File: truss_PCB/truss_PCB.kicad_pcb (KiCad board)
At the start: 2 copper layers, 114.3 x 102.9 mm, 195 parts, among them IC1 BAJ0BC0FP-E2, J1 XT60_60A_male, J10 IN_B, J11 IN_B, J12 Serial IO, J13 IO Header, J14 LV IO, J15 HV IO, J2 LimitSwitch, J3 Servo, J4 Truss Connection, J5 IN_B, J6 IN_B, J7 IN_B, J8 IN_B, J9 IN_B, Q1 BC807, Q2 BC807, Q3 BC807, Q4 BC807, Q5 BC807, Q6 BC807, Q7 BC807, Q8 IRF5305_PBF, U1 HX711, U11 LM2596S-ADJ, U12 AMS1117-5.0, U13 AMS1117-3.3, U2 HX711, U3 HX711, U4 HX711, U5 HX711, U6 HX711, U7 HX711, U8 TXS0108EPW, U9 TXS0108EPW

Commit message: updating truss PCB
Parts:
- removed C28: 680u, Capacitor_SMD:CP_Elec_10x10
- added EC28: 680u, Capacitor_SMD:CP_Elec_10x10, F.Cu at (134.6, 60.8)
- added J16: GND, Connector_PinHeader_2.54mm:PinHeader_1x03_P2.54mm_Vertical, F.Cu at (127.6, 99.7)
- added J17: GND, Connector_PinHeader_2.54mm:PinHeader_1x03_P2.54mm_Vertical, F.Cu at (132.7, 95.9)
- added J18: 12V, Connector_PinHeader_2.54mm:PinHeader_1x01_P2.54mm_Vertical, F.Cu at (141.0, 70.5)
- added J19: 6V, Connector_PinHeader_2.54mm:PinHeader_1x01_P2.54mm_Vertical, F.Cu at (141.0, 81.9)
- added J20: 5V_MCU, Connector_PinHeader_2.54mm:PinHeader_1x01_P2.54mm_Vertical, F.Cu at (141.0, 78.1)
- added J21: 3V3, Connector_PinHeader_2.54mm:PinHeader_1x01_P2.54mm_Vertical, F.Cu at (141.0, 85.7)
- added J22: 10V, Connector_PinHeader_2.54mm:PinHeader_1x01_P2.54mm_Vertical, F.Cu at (141.0, 74.3)
- added R47: 10k, Resistor_SMD:R_0805_2012Metric_Pad1.20x1.40mm_HandSolder, F.Cu at (149.9, 123.8)
- added R48: 10k, Resistor_SMD:R_0805_2012Metric_Pad1.20x1.40mm_HandSolder, F.Cu at (149.9, 126.4)
- added R49: 10k, Resistor_SMD:R_0805_2012Metric_Pad1.20x1.40mm_HandSolder, F.Cu at (149.9, 128.9)
- added R50: 10k, Resistor_SMD:R_0805_2012Metric_Pad1.20x1.40mm_HandSolder, F.Cu at (149.9, 131.4)
- added R51: 10k, Resistor_SMD:R_0805_2012Metric_Pad1.20x1.40mm_HandSolder, F.Cu at (149.9, 134.0)
- J3: footprint Connector_PinHeader_2.54mm:PinHeader_1x03_P2.54mm_Vertical -> Connector_PinHeader_2.54mm:PinHeader_1x01_P2.54mm_Vertical
- N2: moved to B.Cu
- moved D5 7.58 mm to (151.1, 81.9)
- moved D8 7.48 mm to (151.1, 85.7)
- moved D7 7.40 mm to (151.1, 78.1)
- moved D3 7.23 mm to (151.1, 70.5)
- moved D6 7.23 mm to (151.1, 74.3)
- moved JP39 4.44 mm to (151.1, 118.7)
- moved JP38 4.43 mm to (156.2, 118.7)
- moved R43 2.86 mm to (147.1, 85.7)
- moved R40 2.84 mm to (147.0, 81.9)
- moved R42 2.53 mm to (147.1, 78.1)
- moved R41 2.44 mm to (147.1, 74.3)
- moved R39 2.35 mm to (147.1, 70.5)
- moved JP29 0.62 mm to (161.9, 122.6)
- moved G*** 0.51 mm to (144.3, 92.7)
- moved N2 0.43 mm to (156.7, 65.4)
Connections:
- net Net-(A1-Pad1) renamed /MCU/TX
- net Net-(A1-Pad2) renamed /MCU/RX
- A1 pad 24: Net-(A1-Pad24) -> /MCU/LED_2
- A1 pad 25: Net-(A1-Pad25) -> /MCU/LED_3
- A1 pad 26: Net-(A1-Pad26) -> /MCU/LED_4
- D10 pad 2: Net-(A1-Pad25) -> /MCU/LED_3
- D11 pad 2: Net-(A1-Pad26) -> /MCU/LED_4
- D3 pad 1: Net-(D3-Pad1) -> GNDPWR
- D3 pad 2: /Power Distribution/12V_BUS -> Net-(D3-Pad2)
- D5 pad 1: Net-(D5-Pad1) -> GNDPWR
- D5 pad 2: /SERVO_POWER -> Net-(D5-Pad2)
- D6 pad 1: Net-(D6-Pad1) -> GNDPWR
- D6 pad 2: /10V_DC -> Net-(D6-Pad2)
- D7 pad 1: Net-(D7-Pad1) -> GNDPWR
- D7 pad 2: 5VDC -> Net-(D7-Pad2)
- D8 pad 1: Net-(D8-Pad1) -> GNDPWR
- D8 pad 2: 3V3DC -> Net-(D8-Pad2)
- D9 pad 2: Net-(A1-Pad24) -> /MCU/LED_2
- J13 pad 5: Net-(A1-Pad24) -> /MCU/LED_2
- J13 pad 6: Net-(A1-Pad25) -> /MCU/LED_3
- J13 pad 7: Net-(A1-Pad26) -> /MCU/LED_4
- J3 pad 1: /SERVO_PWM -> /SERVO_POWER
- J4 pad 15: unconnected-(J4-Pad15) -> /MCU/SPARE_0
- J4 pad 16: unconnected-(J4-Pad16) -> /MCU/LED_3
- J4 pad 34: unconnected-(J4-Pad34) -> /MCU/LED_2
- J4 pad 35: unconnected-(J4-Pad35) -> /MCU/LED_4
- R39 pad 1: GNDPWR -> Net-(D3-Pad2)
- R39 pad 2: Net-(D3-Pad1) -> /Power Distribution/12V_BUS
- R40 pad 1: GNDPWR -> Net-(D5-Pad2)
- R40 pad 2: Net-(D5-Pad1) -> /SERVO_POWER
- R41 pad 1: GNDPWR -> Net-(D6-Pad2)
- R41 pad 2: Net-(D6-Pad1) -> /10V_DC
- R42 pad 1: GNDPWR -> Net-(D7-Pad2)
- R42 pad 2: Net-(D7-Pad1) -> 5VDC
- R43 pad 1: GNDPWR -> Net-(D8-Pad2)
- R43 pad 2: Net-(D8-Pad1) -> 3V3DC
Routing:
- net GNDPWR: track 162.2 -> 316.5 mm, vias 41 -> 39
- net /SERVO_GND: track 175.9 -> 24.1 mm
- net Net-(A1-Pad24): track 14.7 -> 0.00 mm
- net /MCU/LED_2: track 0.00 -> 14.7 mm
- net Net-(A1-Pad25): track 14.4 -> 0.00 mm
- net /MCU/LED_3: track 0.00 -> 14.4 mm
- net Net-(A1-Pad26): track 14.1 -> 0.00 mm
- net /MCU/LED_4: track 0.00 -> 14.1 mm
- net Net-(J14-Pad1): track 9.14 -> 15.0 mm
- net Net-(J14-Pad5): track 3.60 -> 9.47 mm
- net Net-(J14-Pad4): track 4.16 -> 10.0 mm
- net Net-(J14-Pad3): track 5.36 -> 11.2 mm
- net Net-(J14-Pad2): track 7.25 -> 13.1 mm
- net 5VDC: track 470.6 -> 475.9 mm
- net /10V_DC: track 205.5 -> 210.8 mm
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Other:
- board text added: "LABEL THESE"
- board text added: "RST"
- board text added: "Rx"
- board text added: "Tx"
- board text added: "Vusb"

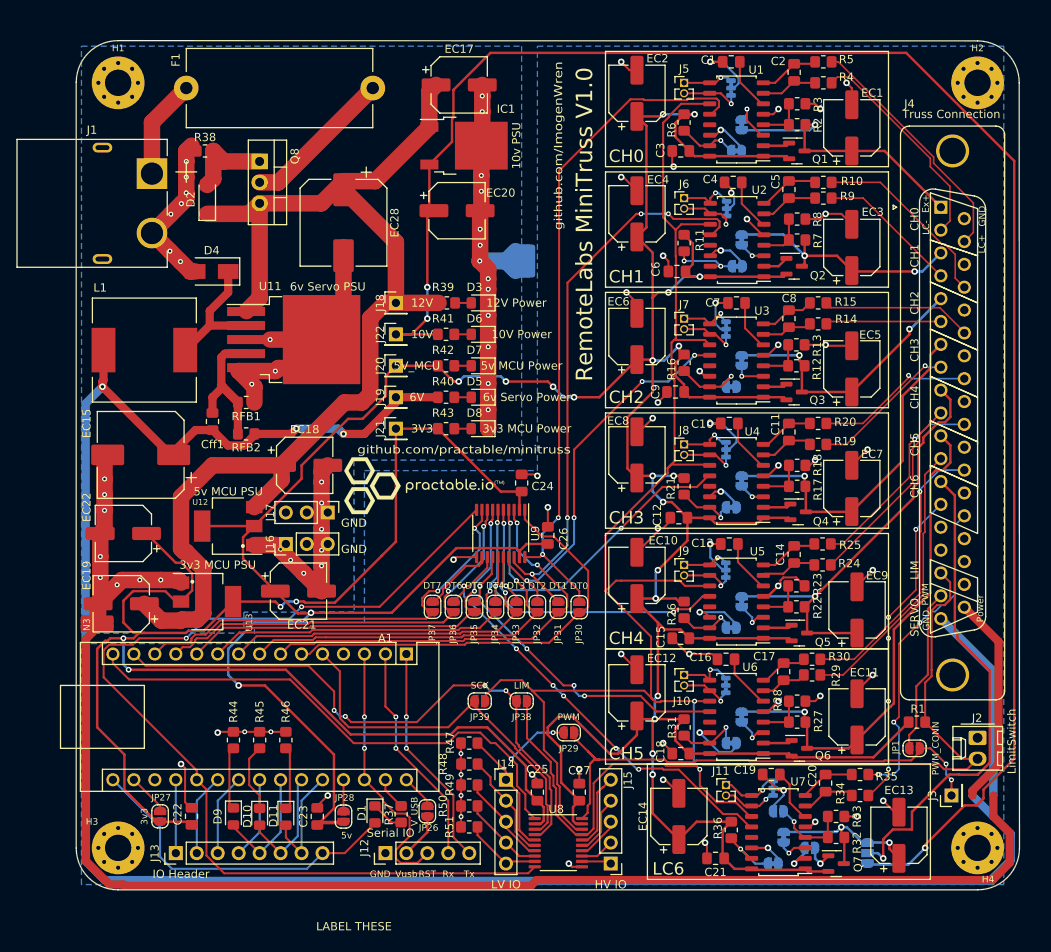
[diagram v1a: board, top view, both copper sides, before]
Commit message: Board V2 Almost Finished TODO# RUN DRC
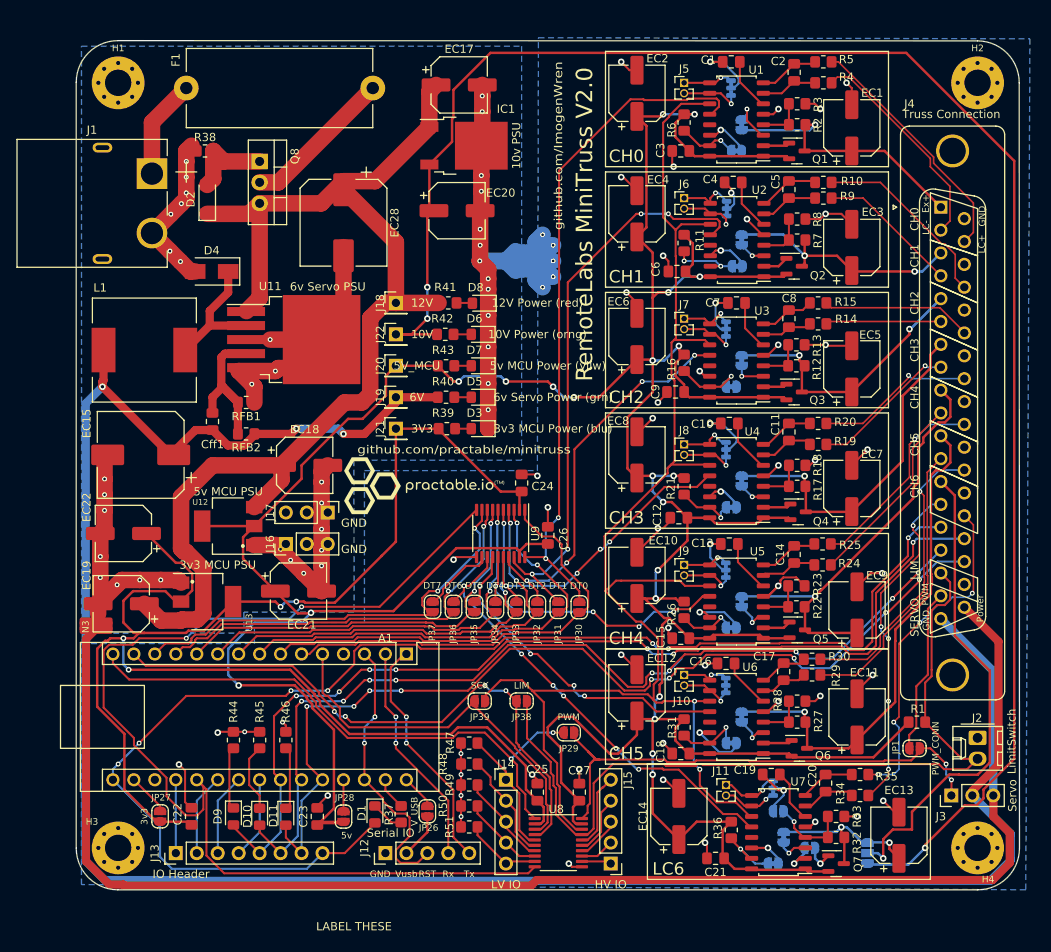
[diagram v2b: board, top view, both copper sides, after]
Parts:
- D3: value 12V Power -> 3v3 MCU Power (blu)
- D5: value 6v Servo Power -> 6v Servo Power (grn)
- D6: value 10V Power -> 10V Power (orng)
- D7: value 5v MCU Power -> 5v MCU Power (yllw)
- D8: value 3v3 MCU Power -> 12V Power (red)
- J3: footprint Connector_PinHeader_2.54mm:PinHeader_1x01_P2.54mm_Vertical -> Connector_PinHeader_2.54mm:PinHeader_1x03_P2.54mm_Vertical
- R39: value 10k -> 330r
- R40: value 1k -> 10k
- R42: value 1k -> 8k2
- R43: value 330r -> 1k
- moved D3 15.2 mm to (151.1, 85.7)
- moved R39 15.2 mm to (147.1, 85.7)
- moved D8 15.2 mm to (151.3, 70.5)
- moved R43 7.62 mm to (147.1, 78.1)
- moved R41 3.82 mm to (147.3, 70.5)
- moved R42 3.81 mm to (147.0, 74.3)
- moved C16 0.51 mm to (181.0, 114.2)
- moved Q5 0.46 mm to (189.6, 110.1)
- moved N3 0.28 mm to (104.6, 109.6)
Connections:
- J3 pad 1: /SERVO_POWER -> /SERVO_PWM
- N3 pad 1: GNDPWR -> (no net)
- N3 pad 2: /SERVO_GND -> (no net)
- R39 pad 2: /Power Distribution/12V_BUS -> 3V3DC
- R41 pad 1: Net-(D6-Pad2) -> Net-(D8-Pad2)
- R41 pad 2: /10V_DC -> /Power Distribution/12V_BUS
- R42 pad 1: Net-(D7-Pad2) -> Net-(D6-Pad2)
- R42 pad 2: 5VDC -> /10V_DC
- R43 pad 1: Net-(D8-Pad2) -> Net-(D7-Pad2)
- R43 pad 2: 3V3DC -> 5VDC
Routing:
- net GNDPWR: track 316.5 -> 164.7 mm
- net /SERVO_GND: track 24.1 -> 175.9 mm
- net /MCU/SPARE_0: track 40.6 -> 163.0 mm, vias 0 -> 7
- net /MCU/LED_2: track 14.7 -> 122.6 mm, vias 0 -> 7
- net /MCU/LED_4: track 14.1 -> 117.1 mm, vias 0 -> 9
- net /MCU/LED_3: track 14.4 -> 116.9 mm, vias 0 -> 9
- net /MCU/OUTPUT_ENABLE: track 123.3 -> 133.4 mm
- net GNDA: track 210.7 -> 220.7 mm, vias 59 -> 65
- net 5VDC: track 475.9 -> 478.9 mm
- net /LoadCell/LC+: track 39.0 -> 41.0 mm, vias 3 -> 4
- net /LoadCell/LC-: track 39.0 -> 41.0 mm
- net /MCU/TX: track 27.3 -> 29.0 mm
- net /BridgeDriver4/D_OUT: track 33.9 -> 35.4 mm, vias 2 -> 4
- net /BridgeDriver5/LC+: track 34.4 -> 35.7 mm
- net /MCU/LIMIT_SWITCH: track 72.9 -> 71.9 mm
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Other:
- board text added: "RemoteLabs MiniTruss V2.0"
- board text removed: "RemoteLabs MiniTruss V1.0"

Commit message: Finished PCB Version 2 Design
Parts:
- added G***: LOGO, 000_Graphics_Immo:practactable.io_symbol_10x10, F.Cu at (130.7, 45.0)
- added G***: LOGO, 000_Graphics_Immo:Remote Labs SN Block, B.Cu at (150.7, 49.8)
- D3: value 3v3 MCU Power (blu) -> 3v3 MCU Power
- D5: value 6v Servo Power (grn) -> 6v Servo Power
- D6: value 10V Power (orng) -> 10V Power
- D7: value 5v MCU Power (yllw) -> 5v MCU Power
- D8: value 12V Power (red) -> 12V Power
- moved N3 0.13 mm to (104.6, 109.5)
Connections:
- N3 pad 1: (no net) -> GNDPWR
- N3 pad 2: (no net) -> /SERVO_GND
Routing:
- net GNDA: track 220.7 -> 226.7 mm
- net /MCU/LED_3: track 116.9 -> 113.7 mm
- net /BridgeDriver3/D_OUT: track 36.3 -> 35.1 mm
- net /MCU/LED_4: track 117.1 -> 115.9 mm
- net /MCU/LED_2: track 122.6 -> 121.7 mm
- net /MCU/DT7: track 53.2 -> 53.8 mm
- net 5VDC: track 478.9 -> 478.4 mm
- net GNDPWR: track 164.7 -> 164.8 mm, vias 39 -> 37
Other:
- board text added: "10v"
- board text added: "HXC/5v"

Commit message: Version 2 pcb complete
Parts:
- removed the G*** at (130.7, 45.0)
- D3: value 3v3 MCU Power -> 3v3 Power
- D5: value 6v Servo Power -> 6v Power
- D7: value 5v MCU Power -> 5v Power
- J20: value 5V_MCU -> 5V
- moved G*** 0.47 mm to (144.8, 92.7)
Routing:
- net /MCU/OUTPUT_ENABLE: track 133.4 -> 128.6 mm
- net Net-(A1-Pad19): track 8.89 -> 12.3 mm
- net Net-(A1-Pad23): track 9.94 -> 12.0 mm
- net /BridgeDriver4/D_OUT: track 34.9 -> 36.7 mm
- net Net-(D9-Pad1): track 7.64 -> 8.69 mm
- net /MCU/RST: track 34.0 -> 35.1 mm
- net /BridgeDriver3/D_OUT: track 35.1 -> 36.0 mm
- net /MCU/LED_4: track 115.9 -> 116.6 mm
- net /MCU/SPARE_0: vias 7 -> 8
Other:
- board text added: "Date: 29/09/2022"
- board text added: "Design: Imogen W. Heard"
- board text added: "JLCJLCJLCJLC"
- board text added: "MiniTruss PCB V2.0"
- board text removed: "LABEL THESE"
